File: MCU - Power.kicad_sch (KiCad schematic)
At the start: 22 parts, among them U6 STM32G474RET6, U7 STM32G474RET6

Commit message: Update Schematic
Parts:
- C30, C36, C37, C39, C45, C46: value 1uF 10V 0402 -> 1uF 10V 0603; footprint Duc_Library:C0402 -> Duc:C0603; symbol Duc-Capacitors:CAP CER 0402 -> Duc-Capacitors:CAP CER 0603; LCSC Part C325464 -> C14663; MPN CC0402KRX5R7BB105 -> CAP CER 0603
- C31, C40: value 4.7uF 16V 0402 -> 4.7uF 16V 0603; footprint Duc_Library:C0402 -> Duc:C0603; symbol Duc-Capacitors:CAP CER 0402 -> Duc-Capacitors:CAP CER 0603; LCSC Part C325464 -> C14663; MPN CC0402KRX5R7BB105 -> CAP CER 0603
- C32, C33, C34, C35, C38, C41, C42, C43, C44, C47: value 100nF 50V 0402 -> 100nF 50V 0603; footprint Duc_Library:C0402 -> Duc:C0603; symbol Duc-Capacitors:CAP CER 0402 -> Duc-Capacitors:CAP CER 0603; LCSC Part C325464 -> C14663; MPN CC0402KRX5R7BB105 -> CAP CER 0603

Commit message: Update Schematic & PCB
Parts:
- L2, L3: footprint Duc_Library:L0805 -> Duc:L0805; symbol Duc_Library:PBBHAQ2012H-102T10 -> Duc-Inductors:PBBHAQ2012H-102T10
- U6, U7: footprint Duc_Library:LQFP-64_L10.0-W10.0-P0.50-LS12.0-BL -> Duc:LQFP-64_L10.0-W10.0-P0.50-LS12.0-BL
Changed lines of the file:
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@@
 	)
 	(symbol
-		(lib_id "Duc_Library:PBBHAQ2012H-102T10")
+		(lib_id "Duc-Inductors:PBBHAQ2012H-102T10")
 		(at 198.12 104.14 0)
 		(unit 1)
@@
 			)
 		)
-		(property "Footprint" "Duc_Library:L0805"
+		(property "Footprint" "Duc:L0805"
 			(at 198.12 111.76 0)
 			(effects
@@
 			)
 		)
-		(property "Description" "300m? 1 �25% 1k?@100MHz 0805 Ferrite Beads and Chips RoHS"
-			(at 198.12 104.14 0)
+		(property "Description" "300mΩ 1 ±25% 1kΩ@100MHz 0805 Ferrite Beads and Chips RoHS"
+			(at 191.77 108.966 0)
 			(effects
 				(font
@@
 			)
 		)
-		(property "Footprint" "Duc_Library:LQFP-64_L10.0-W10.0-P0.50-LS12.0-BL"
+		(property "Footprint" "Duc:LQFP-64_L10.0-W10.0-P0.50-LS12.0-BL"
 			(at 266.7 201.93 0)
 			(effects
@@
 			)
 		)
-		(property "Footprint" "Duc_Library:LQFP-64_L10.0-W10.0-P0.50-LS12.0-BL"
+		(property "Footprint" "Duc:LQFP-64_L10.0-W10.0-P0.50-LS12.0-BL"
 			(at 266.7 118.11 0)
 			(effects
@@
 	)
 	(symbol
-		(lib_id "Duc_Library:PBBHAQ2012H-102T10")
+		(lib_id "Duc-Inductors:PBBHAQ2012H-102T10")
 		(at 198.12 187.96 0)
 		(unit 1)
@@
 			)
 		)
-		(property "Footprint" "Duc_Library:L0805"
+		(property "Footprint" "Duc:L0805"
 			(at 198.12 195.58 0)
 			(effects
@@
 			)
 		)
-		(property "Description" "300m? 1 �25% 1k?@100MHz 0805 Ferrite Beads and Chips RoHS"
-			(at 198.12 187.96 0)
-			(effects
-				(font
+		(property "Description" "300mΩ 1 ±25% 1kΩ@100MHz 0805 Ferrite Beads and Chips RoHS"
+			(at 191.77 192.786 0)
+			(effects
+				(font

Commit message: Update Schematic & PCB
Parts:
- C30, C36, C37, C39, C45, C46: value 1uF 10V 0603 -> CAP CER 0603
- C31, C40: value 4.7uF 16V 0603 -> CAP CER 0603
- C32, C33, C34, C35, C38, C41, C42, C43, C44, C47: value 100nF 50V 0603 -> CAP CER 0603
- FB2: renamed from L2; value PBBHAQ2012H-102T10 -> 1k @ 100MHz
- FB3: renamed from L3; value PBBHAQ2012H-102T10 -> 1k @ 100MHz
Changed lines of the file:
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@@
 		(on_board yes)
 		(dnp no)
-		(property "Reference" "L2"
+		(property "Reference" "FB2"
 			(at 198.12 101.6 0)
 			(effects
@@
 			)
 		)
-		(property "Value" "PBBHAQ2012H-102T10"
+		(property "Value" "1k @ 100MHz"
 			(at 198.12 106.68 0)
 			(effects
@@
 			(project "Master_Hand_Kicad"
 				(path "/f9e05184-c88b-4a88-ae9c-ab2bdb32be7c/c5103ceb-5325-4a84-a025-9638a412984e/f06537ee-772d-44d3-8c50-e0ba41038c9c"
-					(reference "L2")
+					(reference "FB2")
 					(unit 1)
 				)
@@
 			)
 		)
-		(property "Value" "100nF 50V 0603"
+		(property "Value" "CAP CER 0603"
 			(at 170.18 88.9 90)
 			(effects
@@
 		(on_board no)
 		(dnp no)
-		(property "Reference" "#PWR029"
+		(property "Reference" "#PWR29"
 			(at 235.966 146.304 0)
 			(effects
@@
 			(project "Master_Hand_Kicad"
 				(path "/f9e05184-c88b-4a88-ae9c-ab2bdb32be7c/c5103ceb-5325-4a84-a025-9638a412984e/f06537ee-772d-44d3-8c50-e0ba41038c9c"
-					(reference "#PWR029")
+					(reference "#PWR29")
 					(unit 1)
 				)
@@
 			)
 		)
-		(property "Value" "1uF 10V 0603"
+		(property "Value" "CAP CER 0603"
 			(at 213.36 198.12 90)
 			(effects
@@
 			)
 		)
-		(property "Value" "100nF 50V 0603"
+		(property "Value" "CAP CER 0603"
 			(at 236.22 172.72 90)
 			(effects
@@
 		(on_board no)
 		(dnp no)
-		(property "Reference" "#PWR031"
+		(property "Reference" "#PWR31"
 			(at 147.066 170.434 0)
 			(do_not_autoplace yes)
@@
 			(project "Master_Hand_Kicad"
 				(path "/f9e05184-c88b-4a88-ae9c-ab2bdb32be7c/c5103ceb-5325-4a84-a025-9638a412984e/f06537ee-772d-44d3-8c50-e0ba41038c9c"
-					(reference "#PWR031")
+					(reference "#PWR31")
 					(unit 1)
 				)
@@
 			)
 		)
-		(property "Value" "100nF 50V 0603"
+		(property "Value" "CAP CER 0603"
 			(at 193.04 172.72 90)
 			(effects
@@
 			)
 		)
-		(property "Value" "1uF 10V 0603"
+		(property "Value" "CAP CER 0603"
 			(at 177.8 114.3 90)
 			(effects
@@
 			)
 		)
-		(property "Value" "1uF 10V 0603"
+		(property "Value" "CAP CER 0603"
 			(at 236.22 66.04 90)
 			(effects
@@
 		(on_board no)
 		(dnp no)
-		(property "Reference" "#PWR027"
+		(property "Reference" "#PWR27"
 			(at 147.066 86.614 0)
 			(do_not_autoplace yes)
@@
 			(project "Master_Hand_Kicad"
 				(path "/f9e05184-c88b-4a88-ae9c-ab2bdb32be7c/c5103ceb-5325-4a84-a025-9638a412984e/f06537ee-772d-44d3-8c50-e0ba41038c9c"
-					(reference "#PWR027")
+					(reference "#PWR27")
 					(unit 1)
 				)
@@
 		(on_board no)
 		(dnp no)
-		(property "Reference" "#PWR030"
+		(property "Reference" "#PWR30"
 			(at 286.766 166.624 0)
 			(do_not_autoplace yes)
@@
 			(project "Master_Hand_Kicad"
 				(path "/f9e05184-c88b-4a88-ae9c-ab2bdb32be7c/c5103ceb-5325-4a84-a025-9638a412984e/f06537ee-772d-44d3-8c50-e0ba41038c9c"
-					(reference "#PWR030")
+					(reference "#PWR30")
 					(unit 1)
 				)
@@
 			)
 		)
-		(property "Value" "100nF 50V 0603"
+		(property "Value" "CAP CER 0603"
 			(at 236.22 114.3 90)
 			(effects
@@
 		(on_board yes)
 		(dnp no)
-		(property "Reference" "L3"
+		(property "Reference" "FB3"
 			(at 198.12 185.42 0)
 			(effects
@@
 			)
 		)
-		(property "Value" "PBBHAQ2012H-102T10"
+		(property "Value" "1k @ 100MHz"
 			(at 198.12 190.5 0)
 			(effects
@@
 			(project "Master_Hand_Kicad"
 				(path "/f9e05184-c88b-4a88-ae9c-ab2bdb32be7c/c5103ceb-5325-4a84-a025-9638a412984e/f06537ee-772d-44d3-8c50-e0ba41038c9c"
-					(reference "L3")
+					(reference "FB3")
 					(unit 1)
 				)
@@
 			)
 		)
-		(property "Value" "4.7uF 16V 0603"
+		(property "Value" "CAP CER 0603"
 			(at 154.94 172.72 90)
 			(effects
@@
 			)
 		)
-		(property "Value" "100nF 50V 0603"
+		(property "Value" "CAP CER 0603"
 			(at 236.22 198.12 90)
 			(effects
@@
 			)
 		)
-		(property "Value" "100nF 50V 0603"
+		(property "Value" "CAP CER 0603"
 			(at 215.9 172.72 90)
 			(effects
@@
 			)
 		)
-		(property "Value" "100nF 50V 0603"
+		(property "Value" "CAP CER 0603"
 			(at 215.9 88.9 90)
 			(effects
@@
 			)
 		)
-		(property "Value" "1uF 10V 0603"
+		(property "Value" "CAP CER 0603"
 			(at 177.8 198.12 90)
 			(effects
@@
 		(on_board no)
 		(dnp no)
-		(property "Reference" "#PWR028"
+		(property "Reference" "#PWR28"
 			(at 177.546 113.284 0)
 			(do_not_autoplace yes)
@@
 			(project "Master_Hand_Kicad"
 				(path "/f9e05184-c88b-4a88-ae9c-ab2bdb32be7c/c5103ceb-5325-4a84-a025-9638a412984e/f06537ee-772d-44d3-8c50-e0ba41038c9c"
-					(reference "#PWR028")
+					(reference "#PWR28")
 					(unit 1)
 				)
@@
 			)
 		)
-		(property "Value" "100nF 50V 0603"
+		(property "Value" "CAP CER 0603"
 			(at 193.04 88.9 90)
 			(effects
@@
 			)
 		)
-		(property "Value" "1uF 10V 0603"
+		(property "Value" "CAP CER 0603"
 			(at 213.36 114.3 90)
 			(effects
@@
 			)
 		)
-		(property "Value" "1uF 10V 0603"
+		(property "Value" "CAP CER 0603"
 			(at 236.22 149.86 90)
 			(effects
@@
 		(on_board no)
 		(dnp no)
-		(property "Reference" "#PWR025"
+		(property "Reference" "#PWR25"
 			(at 235.966 62.484 0)
 			(effects
@@
 			(project "Master_Hand_Kicad"
 				(path "/f9e05184-c88b-4a88-ae9c-ab2bdb32be7c/c5103ceb-5325-4a84-a025-9638a412984e/f06537ee-772d-44d3-8c50-e0ba41038c9c"
-					(reference "#PWR025")
+					(reference "#PWR25")
 					(unit 1)
 				)
@@
 			)
 		)
-		(property "Value" "100nF 50V 0603"
+		(property "Value" "CAP CER 0603"
 			(at 170.18 172.72 90)
 			(effects
@@
 			)
 		)
-		(property "Value" "100nF 50V 0603"
+		(property "Value" "CAP CER 0603"
 			(at 236.22 88.9 90)
 			(effects
@@
 		(on_board no)
 		(dnp no)
-		(property "Reference" "#PWR026"
+		(property "Reference" "#PWR26"
 			(at 286.766 82.804 0)
 			(do_not_autoplace yes)
@@
 			(project "Master_Hand_Kicad"
 				(path "/f9e05184-c88b-4a88-ae9c-ab2bdb32be7c/c5103ceb-5325-4a84-a025-9638a412984e/f06537ee-772d-44d3-8c50-e0ba41038c9c"
-					(reference "#PWR026")
+					(reference "#PWR26")
 					(unit 1)
 				)
@@
 		(on_board no)
 		(dnp no)
-		(property "Reference" "#PWR032"
+		(property "Reference" "#PWR32"
 			(at 177.546 197.104 0)
 			(do_not_autoplace yes)
@@
 			(project "Master_Hand_Kicad"
 				(path "/f9e05184-c88b-4a88-ae9c-ab2bdb32be7c/c5103ceb-5325-4a84-a025-9638a412984e/f06537ee-772d-44d3-8c50-e0ba41038c9c"
-					(reference "#PWR032")
+					(reference "#PWR32")
 					(unit 1)
 				)
@@
 			)
 		)
-		(property "Value" "4.7uF 16V 0603"
+		(property "Value" "CAP CER 0603"
 			(at 154.94 88.9 90)
 			(effects

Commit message: Update SCH & PCB
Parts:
- renumbered C30 to C25, C31 to C26, C32 to C27, C33 to C28, C34 to C29, C35 to C30, C36 to C31, C37 to C32, C38 to C33, C39 to C34, C40 to C35, C41 to C36, C42 to C37, C43 to C38, C44 to C39, C45 to C40, C46 to C41, C47 to C42, FB2 to FB1, FB3 to FB2
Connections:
- net +3V3: now also C35.1, C36.2, C37.2, C38.2, C39.2, U7.16 (VDD), U7.32 (VDD), U7.48 (VDD), U7.64 (VDD); no longer C40.2, FB2.1
- net +A3V3: now also C40.2, FB2.1; no longer C35.1, C36.2, C37.2, C38.2, C39.2, U7.16 (VDD), U7.32 (VDD), U7.48 (VDD), U7.64 (VDD)

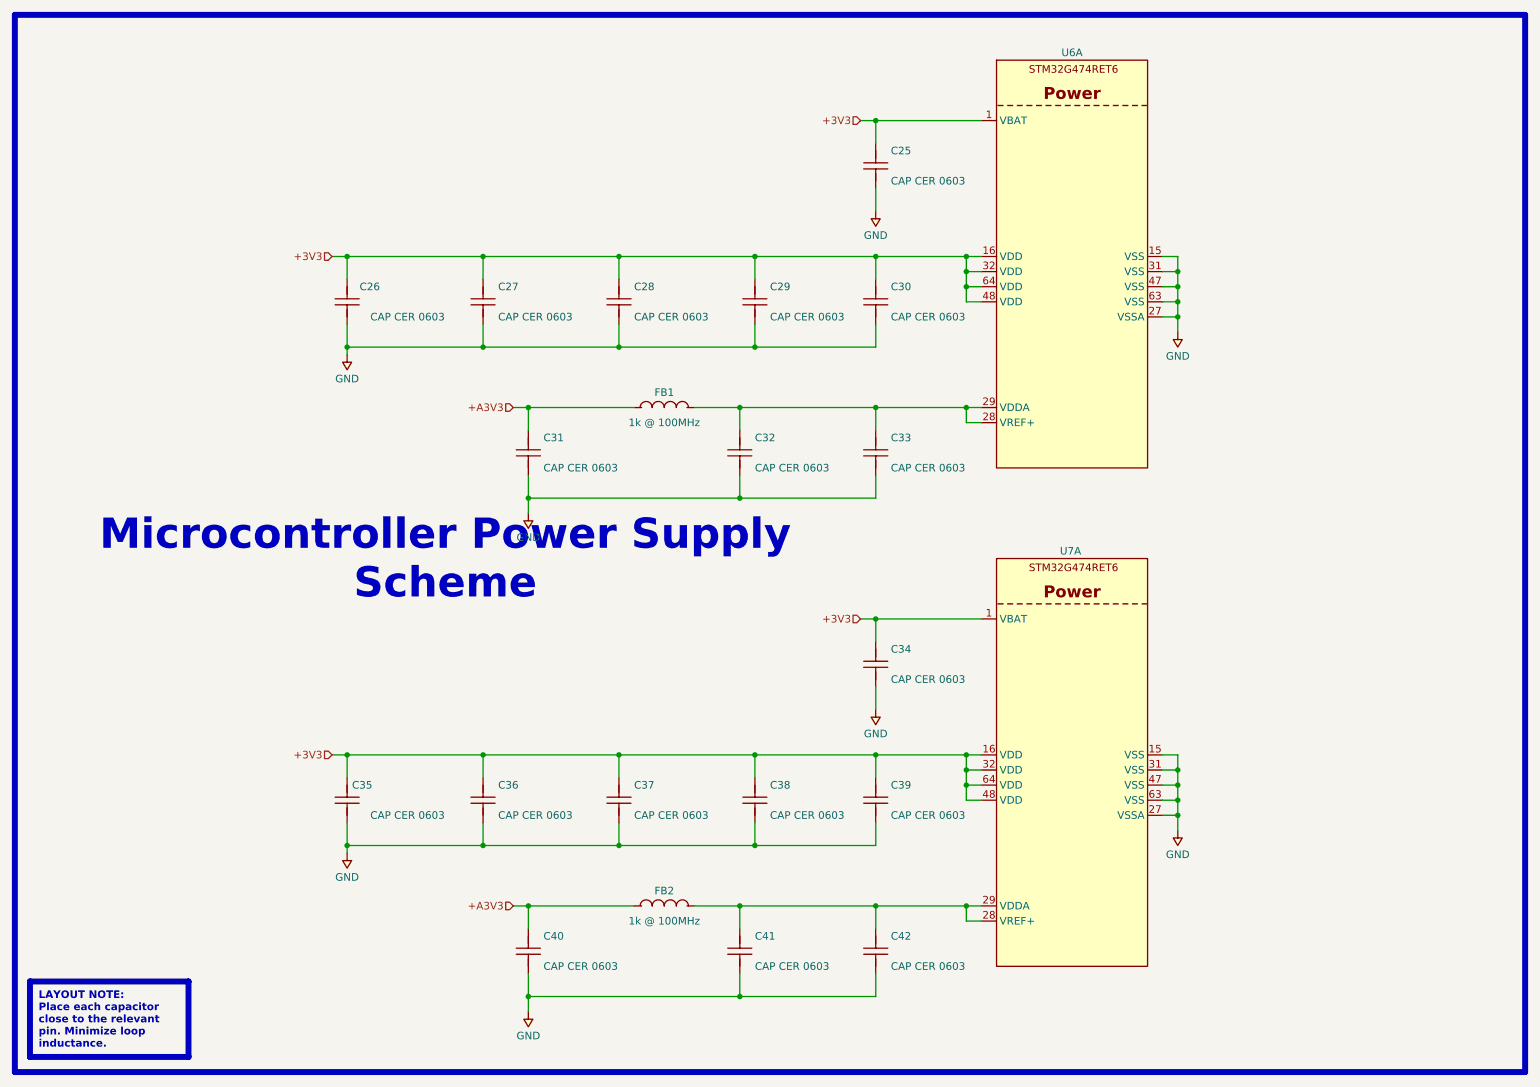
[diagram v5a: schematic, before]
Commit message: Update SCH & PCB & STM32 IOC
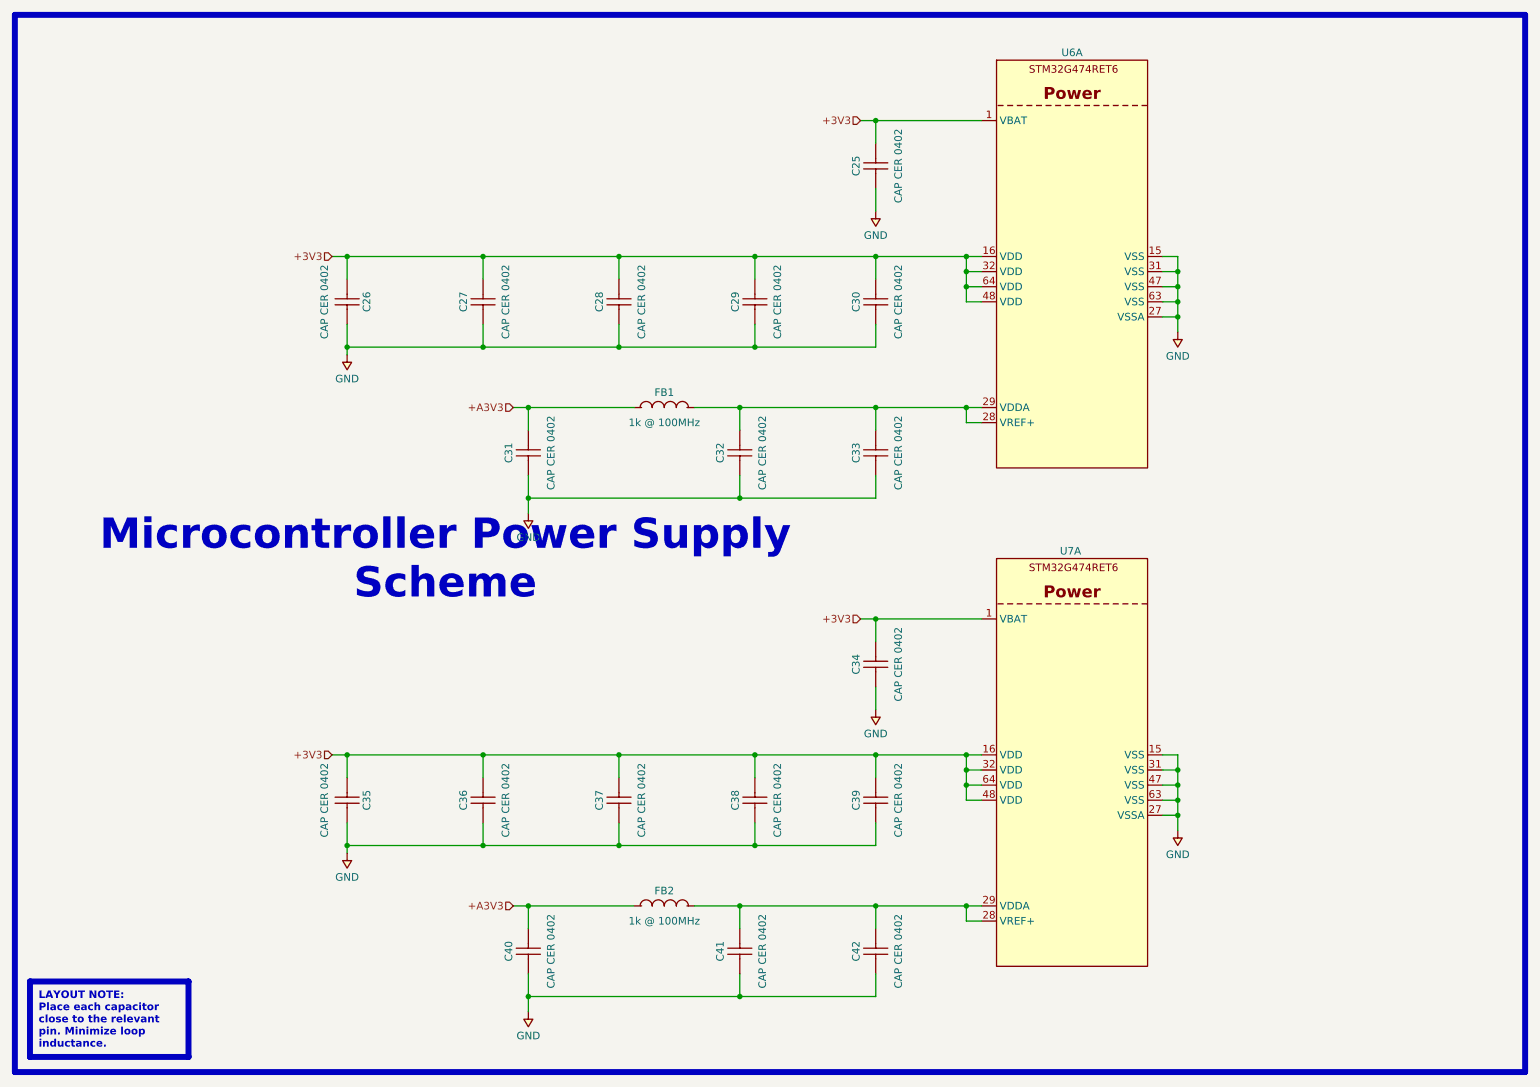
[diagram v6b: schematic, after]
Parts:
- C25, C26, C27, C28, C29, C30, C31, C32, C33, C34, C35, C36, C37, C38, C39, C40, C41, C42: value CAP CER 0603 -> CAP CER 0402; footprint Duc:C0603 -> Duc:C0402; symbol Duc-Capacitors:CAP CER 0603 -> Duc-Capacitors:CAP CER 0402; LCSC Part C14663 -> C325464; MPN CAP CER 0603 -> CC0402KRX5R7BB105
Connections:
- net +3V3: now also C25.1, C26.2, C27.1, C28.1, C29.1, C30.1, C34.1, C35.2, C36.1, C37.1, C38.1, C39.1; no longer C25.2, C26.1, C27.2, C28.2, C29.2, C30.2, C34.2, C35.1, C36.2, C37.2, C38.2, C39.2
- net +A3V3: now also C31.1, C40.1; no longer C31.2, C40.2
- net GND: now also C25.2, C26.1, C27.2, C28.2, C29.2, C30.2, C31.2, C32.2, C33.2, C34.2, C35.1, C36.2, C37.2, C38.2, C39.2, C40.2, C41.2, C42.2; no longer C25.1, C26.2, C27.1, C28.1, C29.1, C30.1, C31.1, C32.1, C33.1, C34.1, C35.2, C36.1, C37.1, C38.1, C39.1, C40.1, C41.1, C42.1
- net at FB1.2, U6.28 (VREF+), U6.29 (VDDA): now also C32.1, C33.1; no longer C32.2, C33.2
- net at FB2.2, U7.28 (VREF+), U7.29 (VDDA): now also C41.1, C42.1; no longer C41.2, C42.2

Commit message: Update Schematic & PCB & STM32 IOC
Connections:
- net +3V3: now also C25.2, C26.1, C27.2, C28.2, C29.2, C30.2, C34.2, C35.1, C36.2, C37.2, C38.2, C39.2; no longer C25.1, C26.2, C27.1, C28.1, C29.1, C30.1, C34.1, C35.2, C36.1, C37.1, C38.1, C39.1
- net +A3V3: now also C31.2, C40.2; no longer C31.1, C40.1
- net GND: now also C25.1, C26.2, C27.1, C28.1, C29.1, C30.1, C31.1, C32.1, C33.1, C34.1, C35.2, C36.1, C37.1, C38.1, C39.1, C40.1, C41.1, C42.1; no longer C25.2, C26.1, C27.2, C28.2, C29.2, C30.2, C31.2, C32.2, C33.2, C34.2, C35.1, C36.2, C37.2, C38.2, C39.2, C40.2, C41.2, C42.2
- net at FB1.2, U6.28 (VREF+), U6.29 (VDDA): now also C32.2, C33.2; no longer C32.1, C33.1
- net at FB2.2, U7.28 (VREF+), U7.29 (VDDA): now also C41.2, C42.2; no longer C41.1, C42.1

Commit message: Update project
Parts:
- C25, C31, C32, C34, C40, C41: value CAP CER 0402 -> 1uF 16V
- C26, C35: value CAP CER 0402 -> 4.7uF 16V
- C27, C28, C29, C30, C33, C36, C37, C38, C39, C42: value CAP CER 0402 -> 100nF 50V
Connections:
- net +3V3: now also C25.1, C27.1, C28.1, C29.1, C30.1, C34.1, C36.1, C37.1, C38.1, C39.1; no longer C25.2, C27.2, C28.2, C29.2, C30.2, C34.2, C36.2, C37.2, C38.2, C39.2
- net +A3V3: now also C31.1, C40.1; no longer C31.2, C40.2
- net GND: now also C25.2, C27.2, C28.2, C29.2, C30.2, C31.2, C32.2, C33.2, C34.2, C36.2, C37.2, C38.2, C39.2, C40.2, C41.2, C42.2; no longer C25.1, C27.1, C28.1, C29.1, C30.1, C31.1, C32.1, C33.1, C34.1, C36.1, C37.1, C38.1, C39.1, C40.1, C41.1, C42.1
- net at FB1.2, U6.28 (VREF+), U6.29 (VDDA): now also C32.1, C33.1; no longer C32.2, C33.2
- net at FB2.2, U7.28 (VREF+), U7.29 (VDDA): now also C41.1, C42.1; no longer C41.2, C42.2
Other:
- moved on the sheet: C25, C27, C28, C29, C30, C31, C32, C33, C34, C36, C37, C38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
